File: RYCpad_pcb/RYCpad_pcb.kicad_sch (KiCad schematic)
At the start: 61 parts, among them J1 USB_C_Receptacle_USB2.0, J2 AVR ISP, K1 KEYSW, K10 KEYSW, K11 KEYSW, K12 KEYSW, K13 KEYSW, K14 KEYSW, K15 KEYSW, K16 KEYSW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

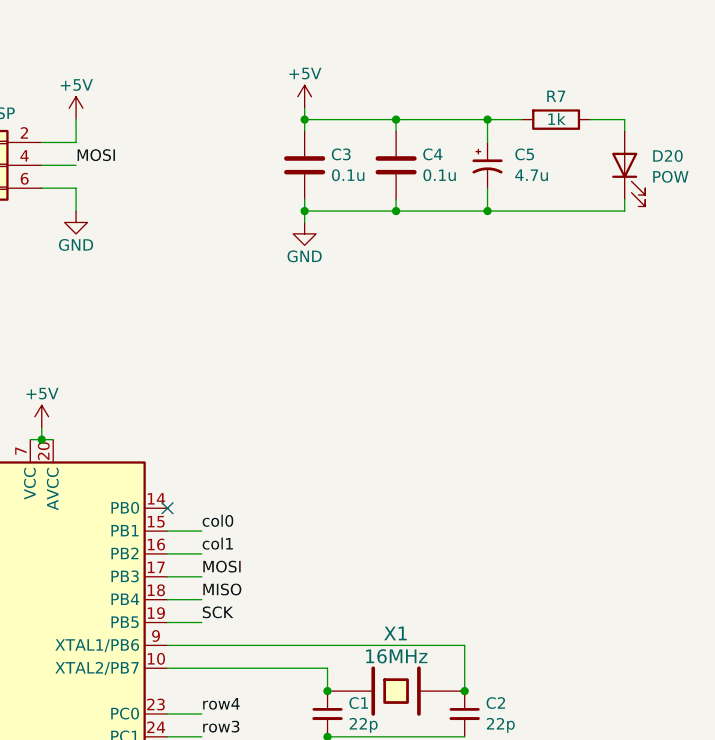
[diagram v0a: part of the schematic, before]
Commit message: Make LED software-controlled
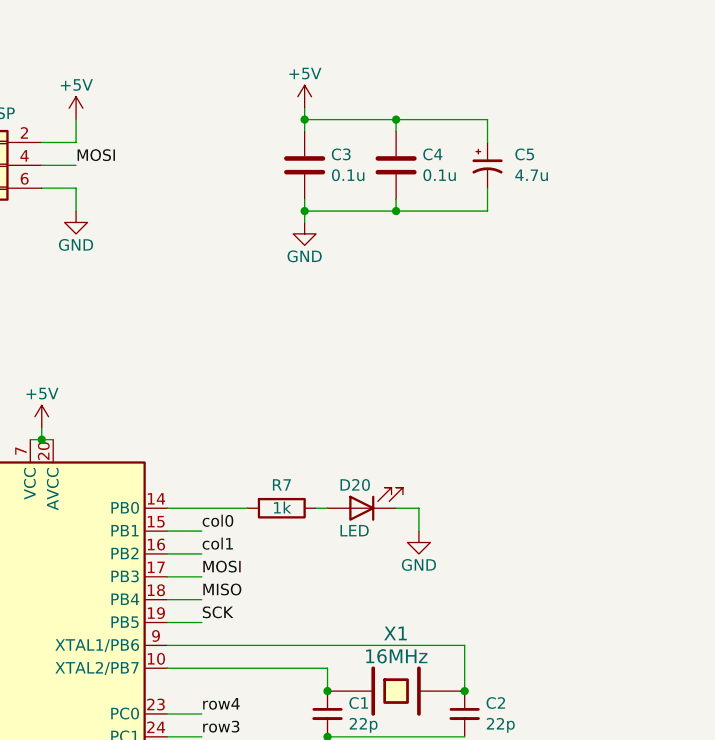
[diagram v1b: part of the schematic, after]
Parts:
- D20: value POW -> LED
- J1: footprint Connector_USB:USB_C_Receptacle_GCT_USB4085 -> personal:USB_C_Receptacle_GCT_USB4085_personalized
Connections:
- net +5V: no longer R7.2
- net at U1.14 (PB0): now also R7.2
- no-connect marks 9 -> 8
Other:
- moved on the sheet: D20, R7
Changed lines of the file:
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@@
   (junction (at 203.2 73.66) (diameter 0) (color 0 0 0 0)
   )
-  (junction (at 252.73 38.1) (diameter 0) (color 0 0 0 0)
-  )
   (junction (at 242.57 48.26) (diameter 0) (color 0 0 0 0)
   )
@@
   )
   (junction (at 105.41 161.29) (diameter 0) (color 0 0 0 0)
-  )
-  (junction (at 252.73 48.26) (diameter 0) (color 0 0 0 0)
   )
   (junction (at 76.2 80.01) (diameter 0) (color 0 0 0 0)
@@
   (no_connect (at 186.69 81.28))
   (no_connect (at 217.17 134.62))
-  (no_connect (at 217.17 81.28))
   (wire (pts (xy 100.33 161.29) (xy 105.41 161.29))
     (stroke (width 0) (type default) (color 0 0 0 0))
@@
     (stroke (width 0) (type default) (color 0 0 0 0))
   )
+  (wire (pts (xy 217.17 81.28) (xy 226.06 81.28))
+    (stroke (width 0) (type default) (color 0 0 0 0))
+  )
   (wire (pts (xy 217.17 91.44) (xy 220.98 91.44))
     (stroke (width 0) (type default) (color 0 0 0 0))
@@
     (stroke (width 0) (type default) (color 0 0 0 0))
   )
-  (wire (pts (xy 267.97 38.1) (xy 267.97 39.37))
-    (stroke (width 0) (type default) (color 0 0 0 0))
-  )
   (wire (pts (xy 101.6 49.53) (xy 81.28 49.53))
     (stroke (width 0) (type default) (color 0 0 0 0))
@@
     (stroke (width 0) (type default) (color 0 0 0 0))
   )
+  (wire (pts (xy 233.68 81.28) (xy 234.95 81.28))
+    (stroke (width 0) (type default) (color 0 0 0 0))
+  )
   (wire (pts (xy 207.01 45.72) (xy 207.01 48.26))
     (stroke (width 0) (type default) (color 0 0 0 0))
@@
     (stroke (width 0) (type default) (color 0 0 0 0))
   )
-  (wire (pts (xy 252.73 38.1) (xy 256.54 38.1))
-    (stroke (width 0) (type default) (color 0 0 0 0))
-  )
   (wire (pts (xy 87.63 163.83) (xy 87.63 166.37))
     (stroke (width 0) (type default) (color 0 0 0 0))
@@
     (stroke (width 0) (type default) (color 0 0 0 0))
   )
+  (wire (pts (xy 242.57 81.28) (xy 245.11 81.28))
+    (stroke (width 0) (type default) (color 0 0 0 0))
+  )
   (wire (pts (xy 102.87 176.53) (xy 105.41 176.53))
     (stroke (width 0) (type default) (color 0 0 0 0))
@@
     (stroke (width 0) (type default) (color 0 0 0 0))
   )
-  (wire (pts (xy 267.97 48.26) (xy 252.73 48.26))
-    (stroke (width 0) (type default) (color 0 0 0 0))
-  )
   (wire (pts (xy 217.17 106.68) (xy 220.98 106.68))
     (stroke (width 0) (type default) (color 0 0 0 0))
@@
     (stroke (width 0) (type default) (color 0 0 0 0))
   )
+  (wire (pts (xy 245.11 81.28) (xy 245.11 83.82))
+    (stroke (width 0) (type default) (color 0 0 0 0))
+  )
   (wire (pts (xy 243.84 142.24) (xy 243.84 143.51))
     (stroke (width 0) (type default) (color 0 0 0 0))
@@
     (stroke (width 0) (type default) (color 0 0 0 0))
   )
-  (wire (pts (xy 267.97 46.99) (xy 267.97 48.26))
-    (stroke (width 0) (type default) (color 0 0 0 0))
-  )
   (wire (pts (xy 232.41 48.26) (xy 232.41 49.53))
     (stroke (width 0) (type default) (color 0 0 0 0))
@@
   )
   (wire (pts (xy 105.41 146.05) (xy 105.41 149.86))
-    (stroke (width 0) (type default) (color 0 0 0 0))
-  )
-  (wire (pts (xy 264.16 38.1) (xy 267.97 38.1))
     (stroke (width 0) (type default) (color 0 0 0 0))
   )
@@
     (property "Reference" "J1" (id 0) (at 75.1078 139.2682 0))
     (property "Value" "USB_C_Receptacle_USB2.0" (id 1) (at 75.1078 141.5796 0))
-    (property "Footprint" "Connector_USB:USB_C_Receptacle_GCT_USB4085" (id 2) (at 76.2 161.29 0)
+    (property "Footprint" "personal:USB_C_Receptacle_GCT_USB4085_personalized" (id 2) (at 76.2 161.29 0)
       (effects (font (size 1.27 1.27)) hide)
     )
@@
     (pin "2")
   )
-  (symbol (lib_id "Device:LED") (at 267.97 43.18 90) (unit 1)
-    (in_bom yes) (on_board yes)
-    (property "Reference" "D20" (id 0) (at 270.9672 42.1894 90)
-      (effects (font (size 1.27 1.27)) (justify right))
-    )
-    (property "Value" "POW" (id 1) (at 270.9672 44.5008 90)
-      (effects (font (size 1.27 1.27)) (justify right))
-    )
-    (property "Footprint" "LED_THT:LED_D3.0mm" (id 2) (at 267.97 43.18 0)
-      (effects (font (size 1.27 1.27)) hide)
-    )
-    (property "Datasheet" "~" (id 3) (at 267.97 43.18 0)
-      (effects (font (size 1.27 1.27)) hide)
-    )
-    (pin "1")
-    (pin "2")
-  )
-  (symbol (lib_id "Device:R") (at 260.35 38.1 270) (unit 1)
-    (in_bom yes) (on_board yes)
-    (property "Reference" "R7" (id 0) (at 260.35 35.56 90))
-    (property "Value" "1k" (id 1) (at 260.35 38.1 90))
-    (property "Footprint" "Resistor_THT:R_Axial_DIN0204_L3.6mm_D1.6mm_P5.08mm_Horizontal" (id 2) (at 260.35 36.322 90)
-      (effects (font (size 1.27 1.27)) hide)
-    )
-    (property "Datasheet" "~" (id 3) (at 260.35 38.1 0)
+  (symbol (lib_id "Device:LED") (at 238.76 81.28 180) (unit 1)
+    (in_bom yes) (on_board yes)
+    (property "Reference" "D20" (id 0) (at 236.22 78.74 0)
+      (effects (font (size 1.27 1.27)) (justify right))
+    )
+    (property "Value" "LED" (id 1) (at 236.22 83.82 0)
+      (effects (font (size 1.27 1.27)) (justify right))
+    )
+    (property "Footprint" "LED_THT:LED_D3.0mm" (id 2) (at 238.76 81.28 0)
+      (effects (font (size 1.27 1.27)) hide)
+    )
+    (property "Datasheet" "~" (id 3) (at 238.76 81.28 0)
+      (effects (font (size 1.27 1.27)) hide)
+    )
+    (pin "1")
+    (pin "2")
+  )
+  (symbol (lib_id "Device:R") (at 229.87 81.28 270) (unit 1)
+    (in_bom yes) (on_board yes)
+    (property "Reference" "R7" (id 0) (at 229.87 78.74 90))
+    (property "Value" "1k" (id 1) (at 229.87 81.28 90))
+    (property "Footprint" "Resistor_THT:R_Axial_DIN0204_L3.6mm_D1.6mm_P5.08mm_Horizontal" (id 2) (at 229.87 79.502 90)
+      (effects (font (size 1.27 1.27)) hide)
+    )
+    (property "Datasheet" "~" (id 3) (at 229.87 81.28 0)
       (effects (font (size 1.27 1.27)) hide)
     )
@@
     (pin "1")
   )
+  (symbol (lib_id "power:GND") (at 245.11 83.82 0) (unit 1)
+    (in_bom yes) (on_board yes)
+    (property "Reference" "#PWR0104" (id 0) (at 245.11 90.17 0)
+      (effects (font (size 1.27 1.27)) hide)
+    )
+    (property "Value" "GND" (id 1) (at 245.11 87.63 0))
+    (property "Footprint" "" (id 2) (at 245.11 83.82 0)
+      (effects (font (size 1.27 1.27)) hide)
+    )
+    (property "Datasheet" "" (id 3) (at 245.11 83.82 0)
+      (effects (font (size 1.27 1.27)) hide)
+    )
+    (pin "1")
+  )
   (sheet_instances
     (path "/" (page "1"))
@@
       (reference "#PWR0103") (unit 1) (value "GND") (footprint "")
     )
+    (path "/1d6119f2-44bf-40a9-8eca-1e6c7ecc0700"
+      (reference "#PWR0104") (unit 1) (value "GND") (footprint "")
+    )
     (path "/00000000-0000-0000-0000-0000608a75fb"
       (reference "C1") (unit 1) (value "22p") (footprint "Capacitor_THT:C_Disc_D3.0mm_W1.6mm_P2.50mm")
@@
     )
     (path "/00000000-0000-0000-0000-000060870c3d"
-      (reference "D20") (unit 1) (value "POW") (footprint "LED_THT:LED_D3.0mm")
+      (reference "D20") (unit 1) (value "LED") (footprint "LED_THT:LED_D3.0mm")
     )
     (path "/00000000-0000-0000-0000-00006086e2e2"
@@
     )
     (path "/00000000-0000-0000-0000-0000608524c1"
-      (reference "J1") (unit 1) (value "USB_C_Receptacle_USB2.0") (footprint "Connector_USB:USB_C_Receptacle_GCT_USB4085")
+      (reference "J1") (unit 1) (value "USB_C_Receptacle_USB2.0") (footprint "personal:USB_C_Receptacle_GCT_USB4085_personalized")
     )
     (path "/00000000-0000-0000-0000-0000608f34fe"

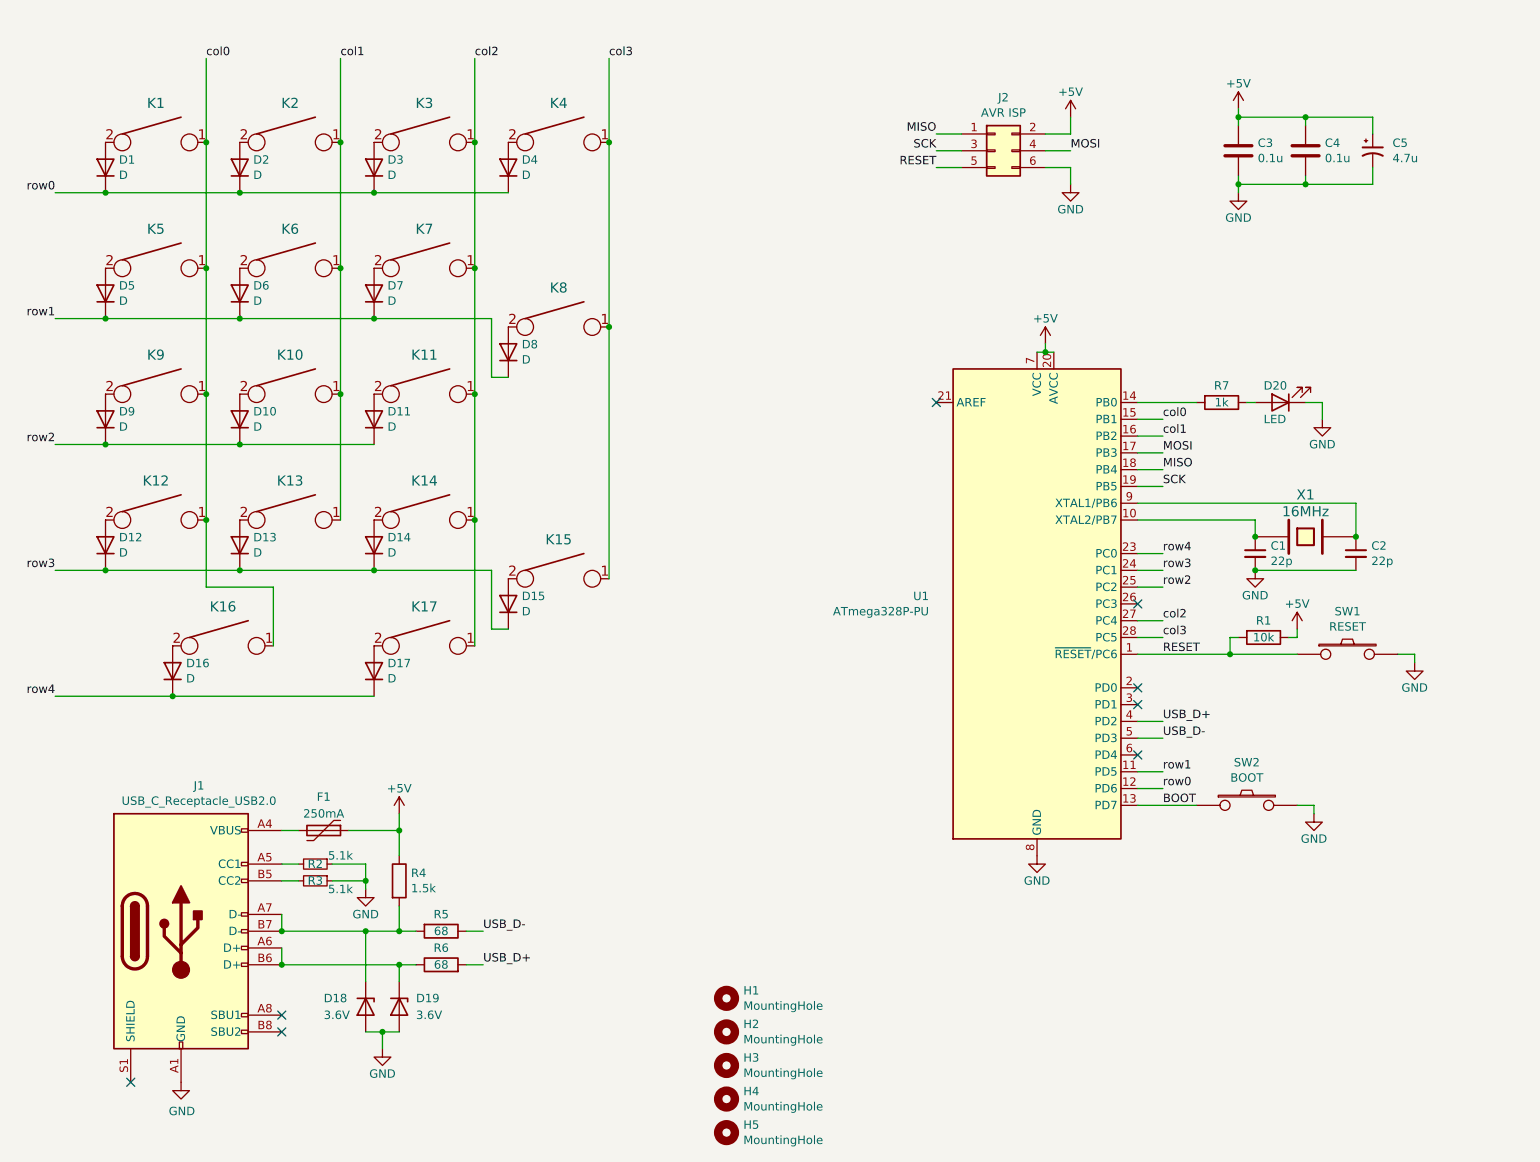
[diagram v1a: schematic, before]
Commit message: connected shield through RC filter
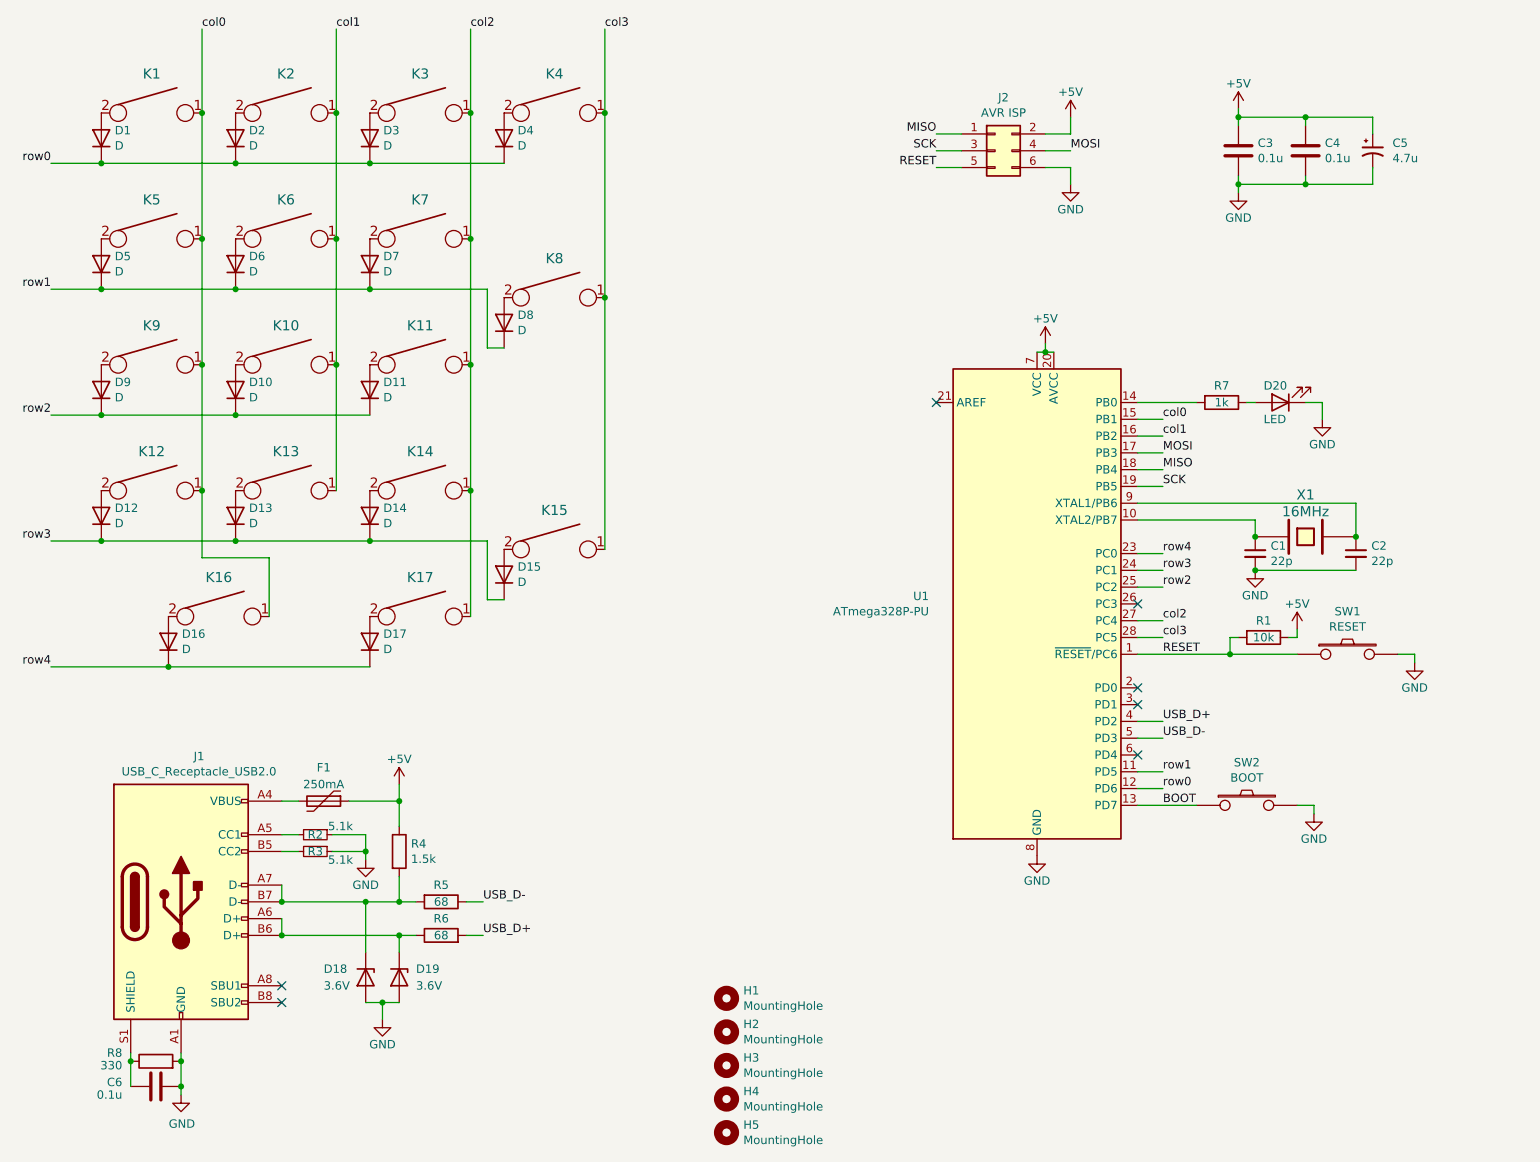
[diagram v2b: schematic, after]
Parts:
- added C6: 0.1u, Capacitor_THT:C_Disc_D4.3mm_W1.9mm_P5.00mm, symbol Device:C
- added R8: 330, Resistor_THT:R_Axial_DIN0204_L3.6mm_D1.6mm_P5.08mm_Horizontal, symbol Device:R
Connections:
- net GND: now also C6.2, R8.2
- net at J1.S1 (SHIELD): now also C6.1, R8.1
- no-connect marks 8 -> 7
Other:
- moved on the sheet: D1, D10, D11, D12, D13, D14, D15, D16, D17, D18, D19, D2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

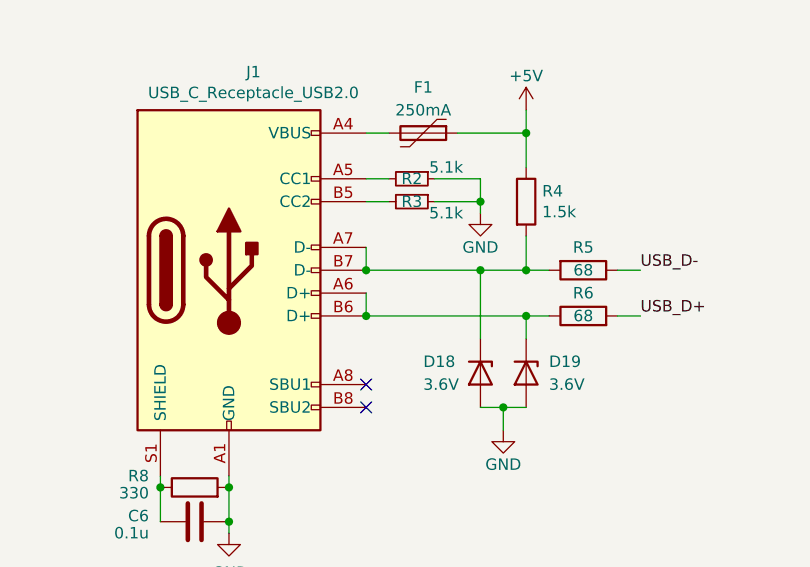
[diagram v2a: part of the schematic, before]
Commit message: matched USB data line length
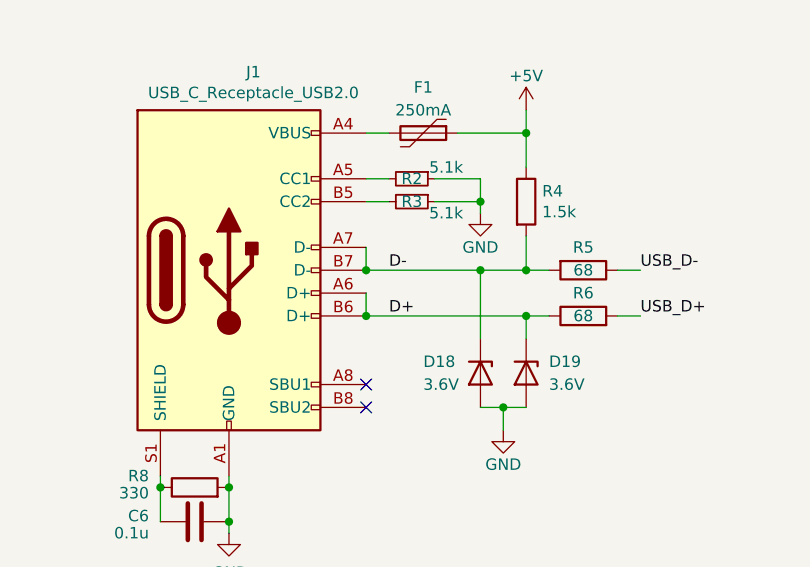
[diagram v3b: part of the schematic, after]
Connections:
- net D+: now reaches D19.1 (K), J1.A6 (D+), J1.B6 (D+), R6.1
- net D-: now reaches D18.1 (K), J1.A7 (D-), J1.B7 (D-), R4.2, R5.2
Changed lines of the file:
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@@
     (stroke (width 0) (type default) (color 0 0 0 0))
+  )
+  (label "D-" (at 90.17 156.845 0)
+    (effects (font (size 1.27 1.27)) (justify left bottom))
   )
   (label "SCK" (at 220.98 93.98 0)
@@
     (effects (font (size 1.27 1.27)) (justify right bottom))
   )
+  (label "D+" (at 90.17 161.925 0)
+    (effects (font (size 1.27 1.27)) (justify left bottom))
+  )
   (label "col1" (at 220.98 86.36 0)
